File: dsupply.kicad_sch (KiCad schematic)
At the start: 74 parts, among them J8 Barrel_Jack, Q3 AOSP21321, Q4 AOSP21321, Q5 AOSP21321, Q6 BC857, Q7 BC857, Q8 BC857, Q9 BC857, U24 PM1202, U25 AMS1117-3.3, U26 TPS54620

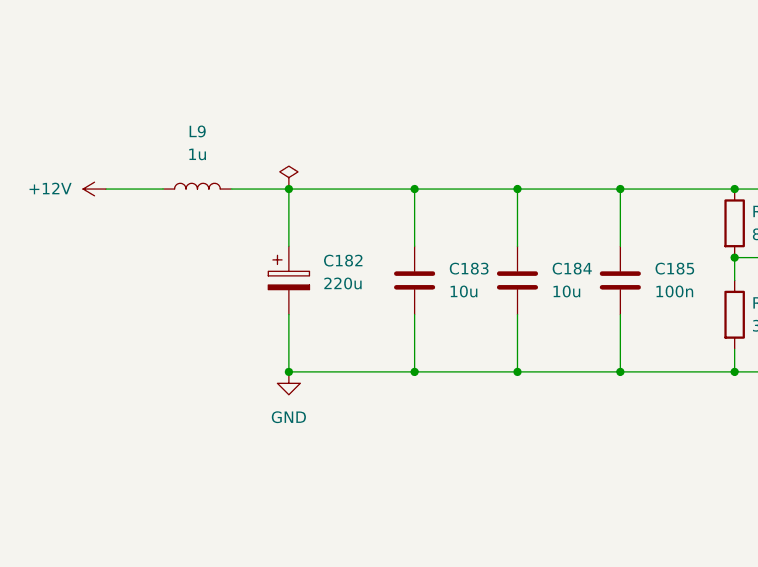
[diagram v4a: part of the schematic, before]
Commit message: sch, pcb: Add TAN Caps to all LT304x SET Pin - Prevent noise due to microphonics to be amplified by internal Amp - Remove the input TAN Caps as LT304x PSRR is very good - Replace TAN Caps in the 12V input side to be ELEC Cap     - Save cost
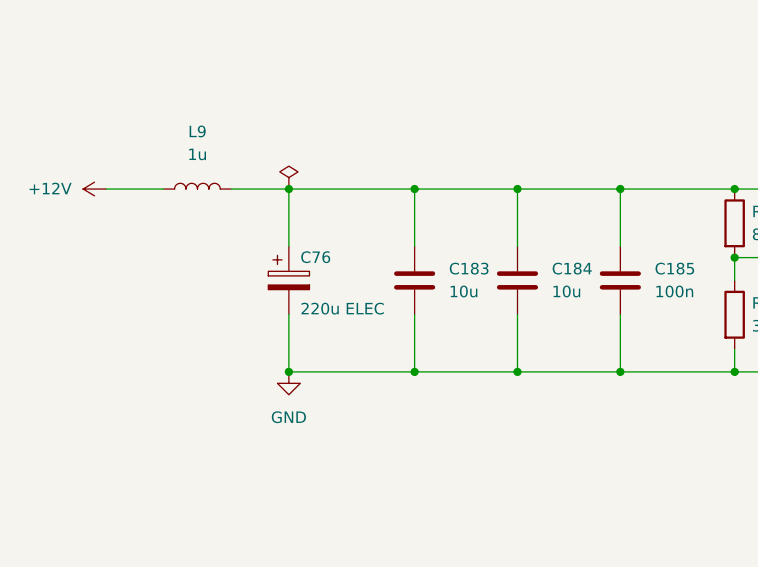
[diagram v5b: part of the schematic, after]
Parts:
- removed C182: 220u, Capacitor_Tantalum_SMD:CP_EIA-7343-15_Kemet-W, symbol Device:C_Polarized
- added C76: 220u ELEC, kirdy:Cap_Elec_SMD_865080345012, symbol Device:C_Polarized
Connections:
- net GND: now also C76.2
- net at C183.1, C184.1, C185.1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: now also C76.1
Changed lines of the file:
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@@
+    )
+  )
+  (symbol (lib_id "Device:C_Polarized") (at 73.66 160.02 0) (unit 1)
+    (in_bom yes) (on_board yes) (dnp no)
+    (property "Reference" "C76" (at 74.93 157.48 0)
+      (effects (font (size 1.27 1.27)) (justify left))
+    )
+    (property "Value" "220u ELEC" (at 74.93 163.195 0)
+      (effects (font (size 1.27 1.27)) (justify left))
+    )
+    (property "Footprint" "kirdy:Cap_Elec_SMD_865080345012" (at 74.6252 163.83 0)
+      (effects (font (size 1.27 1.27)) hide)
+    )
+    (property "Datasheet" "~" (at 73.66 160.02 0)
+      (effects (font (size 1.27 1.27)) hide)
+    )
+    (property "MFR_PN" "865080345012" (at 73.66 160.02 0)
+      (effects (font (size 1.27 1.27)) hide)
+    )
+    (pin "1")
+    (pin "2")
+    (instances
+      (project "kirdy"
+        (path "/88da1dd8-9274-4b55-84fb-90006c9b6e8f/b6f53a06-e1b9-4c20-8fc0-ae2d1ce0191d"
+          (reference "C76") (unit 1)
+        )
+      )
     )
   )
@@
         )
       )
-    )
-  )
-  (symbol (lib_id "Device:C_Polarized") (at 73.66 160.02 0) (unit 1)
-    (in_bom yes) (on_board yes) (dnp no) (fields_autoplaced)
-    (property "Reference" "C182" (at 77.47 157.8609 0)
-      (effects (font (size 1.27 1.27)) (justify left))
-    )
-    (property "Value" "220u" (at 77.47 160.4009 0)
-      (effects (font (size 1.27 1.27)) (justify left))
-    )
-    (property "Footprint" "Capacitor_Tantalum_SMD:CP_EIA-7343-15_Kemet-W" (at 74.6252 163.83 0)
-      (effects (font (size 1.27 1.27)) hide)
-    )
-    (property "Datasheet" "~" (at 73.66 160.02 0)
-      (effects (font (size 1.27 1.27)) hide)
-    )
-    (property "MFR_PN" "T491D227K016AT" (at 73.66 160.02 0)
-      (effects (font (size 1.27 1.27)) hide)
-    )
-    (property "MFR_PN_ALT" "293D227X9016E2TE3" (at 73.66 160.02 0)
-      (effects (font (size 1.27 1.27)) hide)
-    )
-    (pin "1")
-    (pin "2")
-    (instances
-      (project "kirdy"
-        (path "/88da1dd8-9274-4b55-84fb-90006c9b6e8f/b6f53a06-e1b9-4c20-8fc0-ae2d1ce0191d"
-          (reference "C182") (unit 1)
-        )
-      )

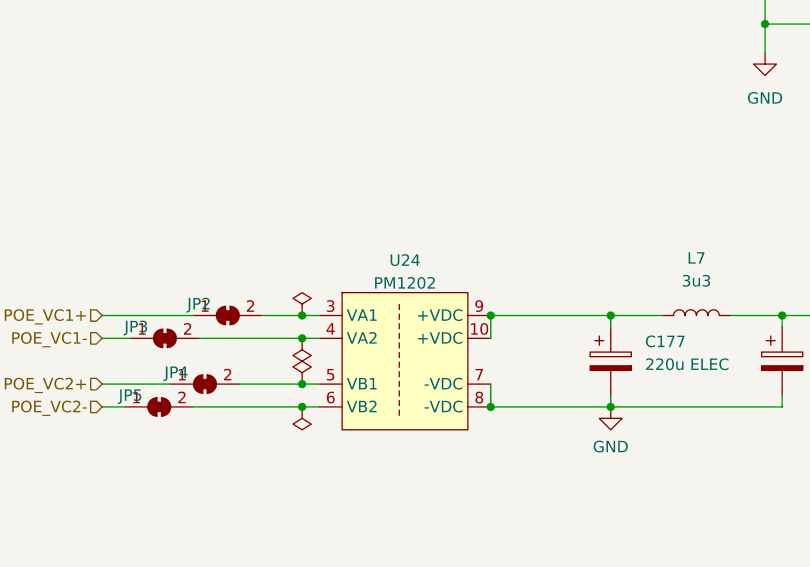
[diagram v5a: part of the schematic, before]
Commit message: Add Manufacturer into PM1202's Value & Comment
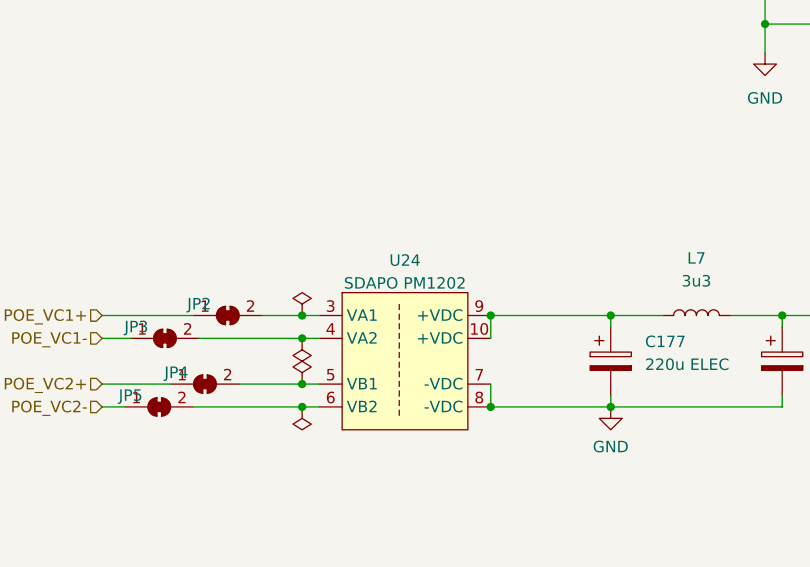
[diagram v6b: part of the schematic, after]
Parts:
- U24: value PM1202 -> SDAPO PM1202; Comment (none) -> Manufacturer: SDAPO
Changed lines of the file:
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@@
       (effects (font (size 1.27 1.27)))
     )
-    (property "Value" "PM1202" (at 156.21 72.6241 0)
+    (property "Value" "SDAPO PM1202" (at 156.21 72.6241 0)
       (effects (font (size 1.27 1.27)))
     )
@@
       (effects (font (size 1.27 1.27)) hide)
     )
+    (property "Comment" "Manufacturer: SDAPO" (at 155.575 83.82 0)
+      (effects (font (size 1.27 1.27)) hide)
+    )

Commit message: sch: Not to include TPs in BOM. Add prod comments - LTC6655 Vref adds production comments
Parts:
- TP? (x4): now left out of the parts list
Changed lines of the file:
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@@
   )
   (symbol (lib_id "Connector:TestPoint") (at 356.87 203.2 90) (unit 1)
-    (in_bom yes) (on_board yes) (dnp no)
+    (in_bom no) (on_board yes) (dnp no)
     (property "Reference" "TP?" (at 354.965 200.66 90)
       (effects (font (size 1.27 1.27)) (justify left))
@@
   )
   (symbol (lib_id "Connector:TestPoint") (at 214.63 74.93 0) (unit 1)
-    (in_bom yes) (on_board yes) (dnp no)
+    (in_bom no) (on_board yes) (dnp no)
     (property "Reference" "TP?" (at 212.09 69.215 0)
       (effects (font (size 1.27 1.27)) (justify left))
@@
   )
   (symbol (lib_id "Connector:TestPoint") (at 356.87 191.77 90) (unit 1)
-    (in_bom yes) (on_board yes) (dnp no)
+    (in_bom no) (on_board yes) (dnp no)
     (property "Reference" "TP?" (at 354.965 189.23 90)
       (effects (font (size 1.27 1.27)) (justify left))
@@
   )
   (symbol (lib_id "Connector:TestPoint") (at 356.87 198.12 90) (unit 1)
-    (in_bom yes) (on_board yes) (dnp no)
+    (in_bom no) (on_board yes) (dnp no)
     (property "Reference" "TP?" (at 354.965 195.58 90)
       (effects (font (size 1.27 1.27)) (justify left))

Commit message: sch: Update PN and Comments
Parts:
- U24: Comment Manufacturer: SDAPO -> https://m.tb.cn/h.5mqugBw?tk=N0blWf9e2cn
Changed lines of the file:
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@@
       (effects (font (size 1.27 1.27)) hide)
     )
-    (property "Comment" "Manufacturer: SDAPO" (at 155.575 83.82 0)
+    (property "Comment" "https://m.tb.cn/h.5mqugBw?tk=N0blWf9e2cn" (at 155.575 83.82 0)
       (effects (font (size 1.27 1.27)) hide)
     )
